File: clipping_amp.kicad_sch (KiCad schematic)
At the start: 14 parts, among them SW1 1MS1T1B1M2QES, U2 TL074

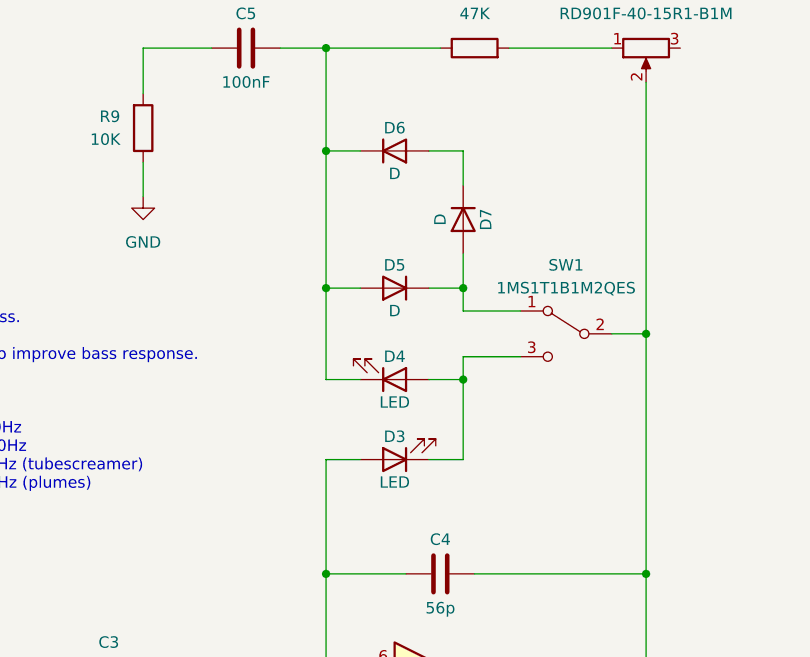
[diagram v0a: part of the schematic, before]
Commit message: added LCSC part numbers
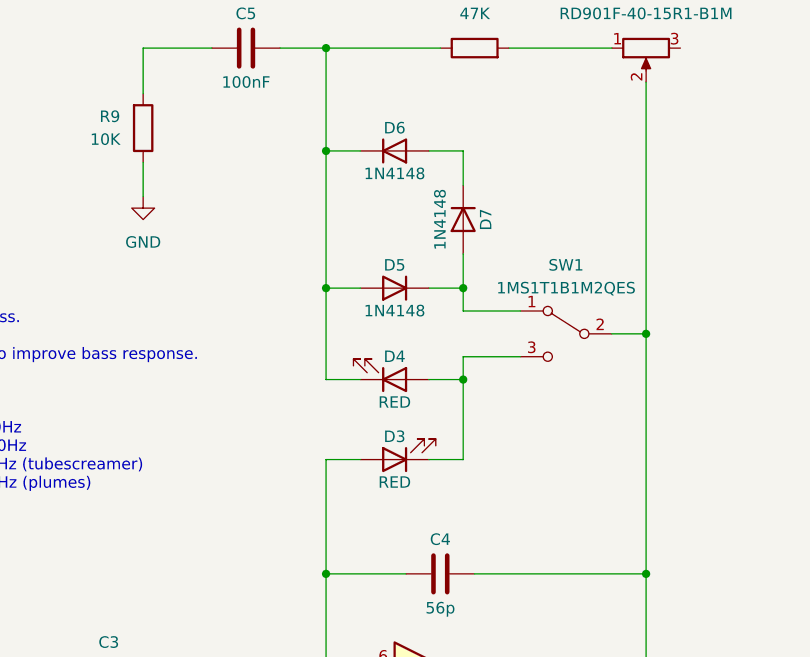
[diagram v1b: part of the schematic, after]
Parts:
- C5: LCSC (none) -> C476766
- D3, D4: value LED -> RED; footprint (none) -> LED_SMD:LED_0805_2012Metric_Pad1.15x1.40mm_HandSolder; LCSC (none) -> C965812
- D5, D6, D7: value D -> 1N4148; footprint (none) -> Diode_SMD:D_SOD-123; LCSC (none) -> C917030
- R7, R9: LCSC (none) -> C2930231
- R8: LCSC (none) -> C2907330
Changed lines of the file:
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@@
       (effects (font (size 1.27 1.27)))
     )
-    (property "Value" "D" (at 146.05 72.39 0)
-      (effects (font (size 1.27 1.27)))
-    )
-    (property "Footprint" "" (at 148.59 72.39 0)
+    (property "Value" "1N4148" (at 146.05 72.39 0)
+      (effects (font (size 1.27 1.27)))
+    )
+    (property "Footprint" "Diode_SMD:D_SOD-123" (at 148.59 72.39 0)
       (effects (font (size 1.27 1.27)) hide)
     )
@@
       (effects (font (size 1.27 1.27)) hide)
     )
+    (property "LCSC" "C917030" (at 148.59 72.39 0)
+      (effects (font (size 1.27 1.27)) hide)
+    )
     (pin "1")
     (pin "2")
@@
       (effects (font (size 1.27 1.27)))
     )
-    (property "Value" "LED" (at 140.97 92.71 0)
-      (effects (font (size 1.27 1.27)))
-    )
-    (property "Footprint" "" (at 140.97 90.17 0)
+    (property "Value" "RED" (at 140.97 92.71 0)
+      (effects (font (size 1.27 1.27)))
+    )
+    (property "Footprint" "LED_SMD:LED_0805_2012Metric_Pad1.15x1.40mm_HandSolder" (at 140.97 90.17 0)
       (effects (font (size 1.27 1.27)) hide)
     )
@@
       (effects (font (size 1.27 1.27)) hide)
     )
+    (property "LCSC" "C965812" (at 140.97 90.17 0)
+      (effects (font (size 1.27 1.27)) hide)
+    )
     (pin "1")
     (pin "2")
@@
       (effects (font (size 1.27 1.27)))
     )
-    (property "Value" "D" (at 140.97 67.31 0)
-      (effects (font (size 1.27 1.27)))
-    )
-    (property "Footprint" "" (at 140.97 64.77 0)
+    (property "Value" "1N4148" (at 140.97 67.31 0)
+      (effects (font (size 1.27 1.27)))
+    )
+    (property "Footprint" "Diode_SMD:D_SOD-123" (at 140.97 64.77 0)
       (effects (font (size 1.27 1.27)) hide)
     )
@@
       (effects (font (size 1.27 1.27)) hide)
     )
+    (property "LCSC" "C917030" (at 140.97 64.77 0)
+      (effects (font (size 1.27 1.27)) hide)
+    )
     (pin "1")
     (pin "2")
@@
       (effects (font (size 1.27 1.27)) hide)
     )
-    (property "LCSC" "" (at 124.46 53.34 0)
+    (property "LCSC" "C476766" (at 124.46 53.34 0)
       (effects (font (size 1.27 1.27)) hide)
     )
@@
       (effects (font (size 1.27 1.27)))
     )
-    (property "Value" "LED" (at 140.97 101.6 0)
-      (effects (font (size 1.27 1.27)))
-    )
-    (property "Footprint" "" (at 140.97 99.06 0)
+    (property "Value" "RED" (at 140.97 101.6 0)
+      (effects (font (size 1.27 1.27)))
+    )
+    (property "Footprint" "LED_SMD:LED_0805_2012Metric_Pad1.15x1.40mm_HandSolder" (at 140.97 99.06 0)
       (effects (font (size 1.27 1.27)) hide)
     )
     (property "Datasheet" "~" (at 140.97 99.06 0)
+      (effects (font (size 1.27 1.27)) hide)
+    )
+    (property "LCSC" "C965812" (at 140.97 99.06 0)
       (effects (font (size 1.27 1.27)) hide)
     )
@@
       (effects (font (size 1.27 1.27)) hide)
     )
+    (property "LCSC" "C2930231" (at 125.73 135.89 0)
+      (effects (font (size 1.27 1.27)) hide)
+    )
     (pin "1")
     (pin "2")
@@
       (effects (font (size 1.27 1.27)) hide)
     )
+    (property "LCSC" "C2907330" (at 149.86 53.34 0)
+      (effects (font (size 1.27 1.27)) hide)
+    )
     (pin "1")
     (pin "2")
@@
       (effects (font (size 1.27 1.27)) hide)
     )
+    (property "LCSC" "~" (at 168.91 53.34 0)
+      (effects (font (size 1.27 1.27)) hide)
+    )
     (pin "1")
     (pin "2")
@@
       (effects (font (size 1.27 1.27)))
     )
-    (property "Value" "D" (at 140.97 82.55 0)
-      (effects (font (size 1.27 1.27)))
-    )
-    (property "Footprint" "" (at 140.97 80.01 0)
+    (property "Value" "1N4148" (at 140.97 82.55 0)
+      (effects (font (size 1.27 1.27)))
+    )
+    (property "Footprint" "Diode_SMD:D_SOD-123" (at 140.97 80.01 0)
       (effects (font (size 1.27 1.27)) hide)
     )
@@
     )
     (property "Sim.Pins" "1=K 2=A" (at 140.97 80.01 0)
+      (effects (font (size 1.27 1.27)) hide)
+    )
+    (property "LCSC" "C917030" (at 140.97 80.01 0)
       (effects (font (size 1.27 1.27)) hide)
     )
@@
       (effects (font (size 1.27 1.27)) hide)
     )
+    (property "LCSC" "C2930231" (at 113.03 62.23 0)
+      (effects (font (size 1.27 1.27)) hide)
+    )
     (pin "1")
     (pin "2")
@@
       (effects (font (size 1.27 1.27)) hide)
     )
+    (property "LCSC" "~" (at 160.02 85.09 0)
+      (effects (font (size 1.27 1.27)) hide)
+    )
+    (property "TAYDA" "~" (at 160.02 85.09 0)
+      (effects (font (size 1.27 1.27)) hide)
+    )

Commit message: added schema pdf
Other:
- title: (none) -> EQD Plume Clone
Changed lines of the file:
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@@
 (kicad_sch (version 20230121) (generator eeschema)
   (paper "A4")
+  (title_block
+    (title "EQD Plume Clone")
+    (date "2023-08-31")
+    (rev "A")
+  )
   (junction (at 125.73 127) (diameter 0) (color 0 0 0 0)
   )
